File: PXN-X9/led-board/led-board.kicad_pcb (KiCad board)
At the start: 2 copper layers, 151 x 100 mm, 35 parts, among them J1 Conn_01x03, U1 74AHCT1G32SE-7, U10 LTST-A683CEGBW1, U11 LTST-A683CEGBW1, U12 LTST-A683CEGBW1, U13 LTST-A683CEGBW1, U14 LTST-A683CEGBW1, U15 LTST-A683CEGBW1, U16 LTST-A683CEGBW1, U17 LTST-A683CEGBW1, U2 LTST-A683CEGBW1, U3 LTST-A683CEGBW1, U4 LTST-A683CEGBW1, U5 LTST-A683CEGBW1, U6 LTST-A683CEGBW1, U7 LTST-A683CEGBW1, U8 LTST-A683CEGBW1, U9 LTST-A683CEGBW1

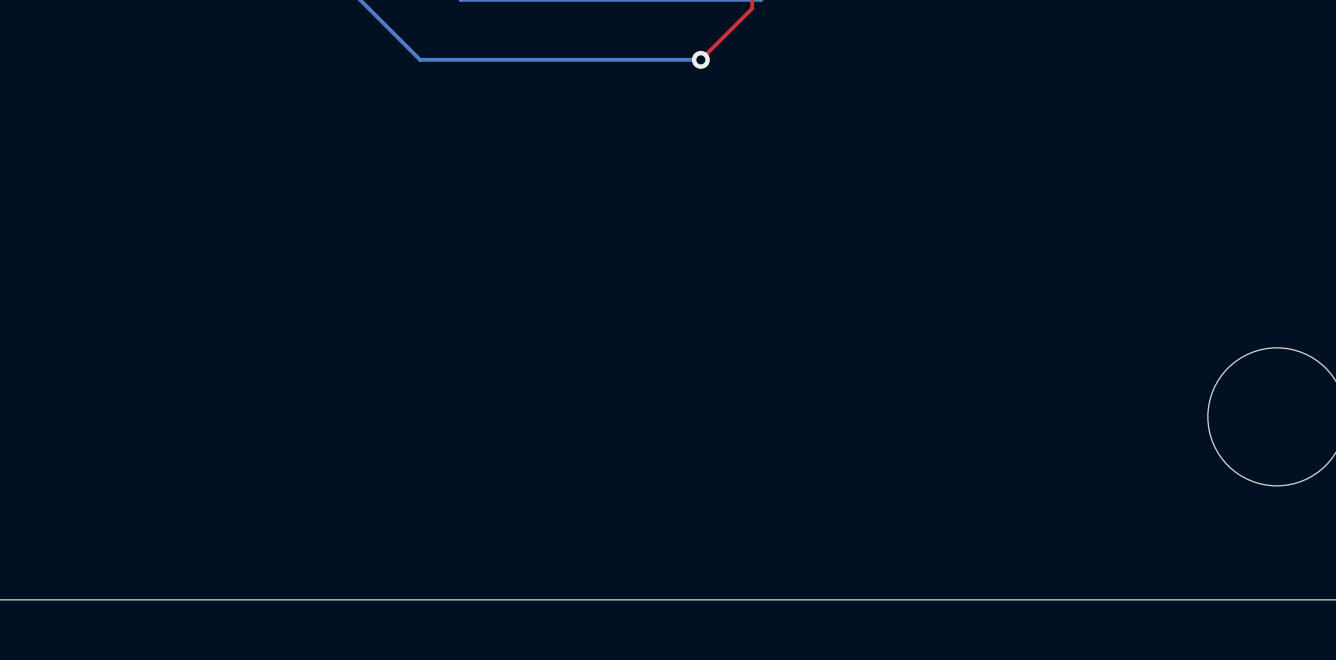
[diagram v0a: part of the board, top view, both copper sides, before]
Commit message: Add Logo to PXN-X9 LED Board
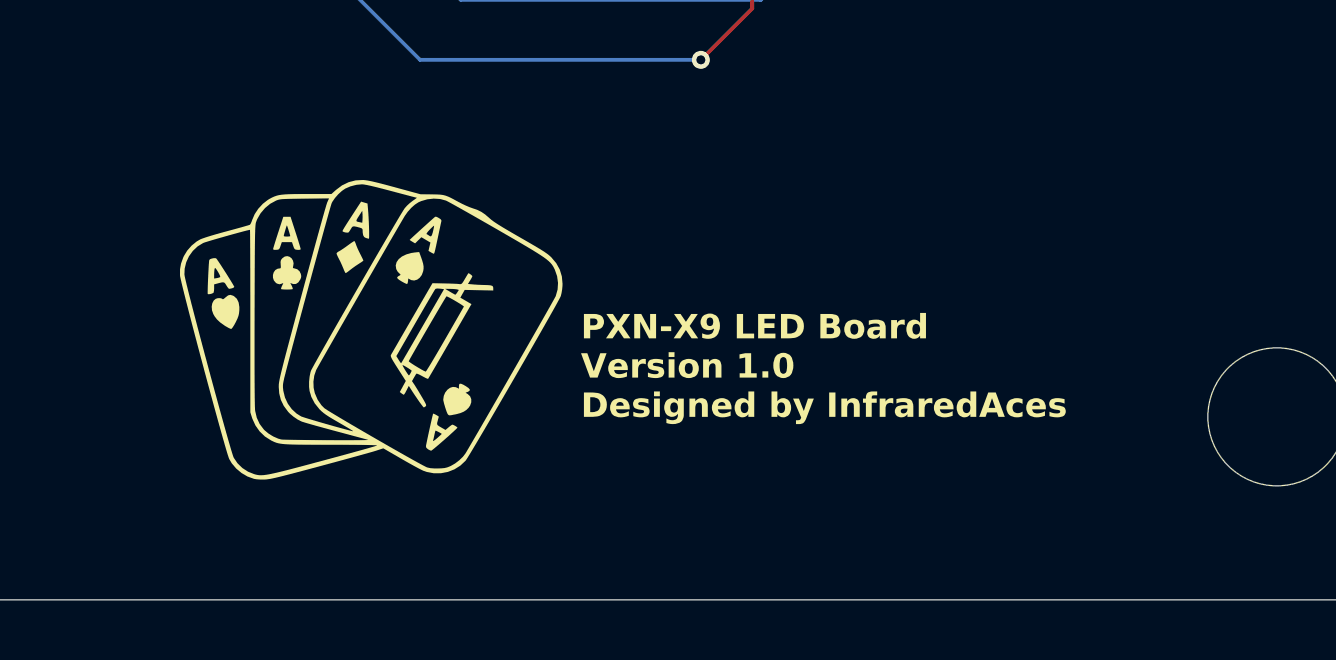
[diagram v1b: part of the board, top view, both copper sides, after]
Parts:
- added G***: LOGO, Logo:InfraredAces-logo, F.Cu at (165.0, 141.0)
- added G***: LOGO, Logo:InfraredAces-logo, B.Cu at (181.5, 141.0)
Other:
- board text added: "PXN-X9 LED Board Version 1.0 Designed by InfraredAces"
